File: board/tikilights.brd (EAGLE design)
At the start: 108.6 x 73 mm, 42 parts, among them IC1 AZ1117EH-3.3TRG1, SW1 ROTARTY_ENCODER, SW2 ROTARTY_ENCODER, SW3 ENCODER_SW1-PEC12, SW4 ENCODER_SW1-PEC12

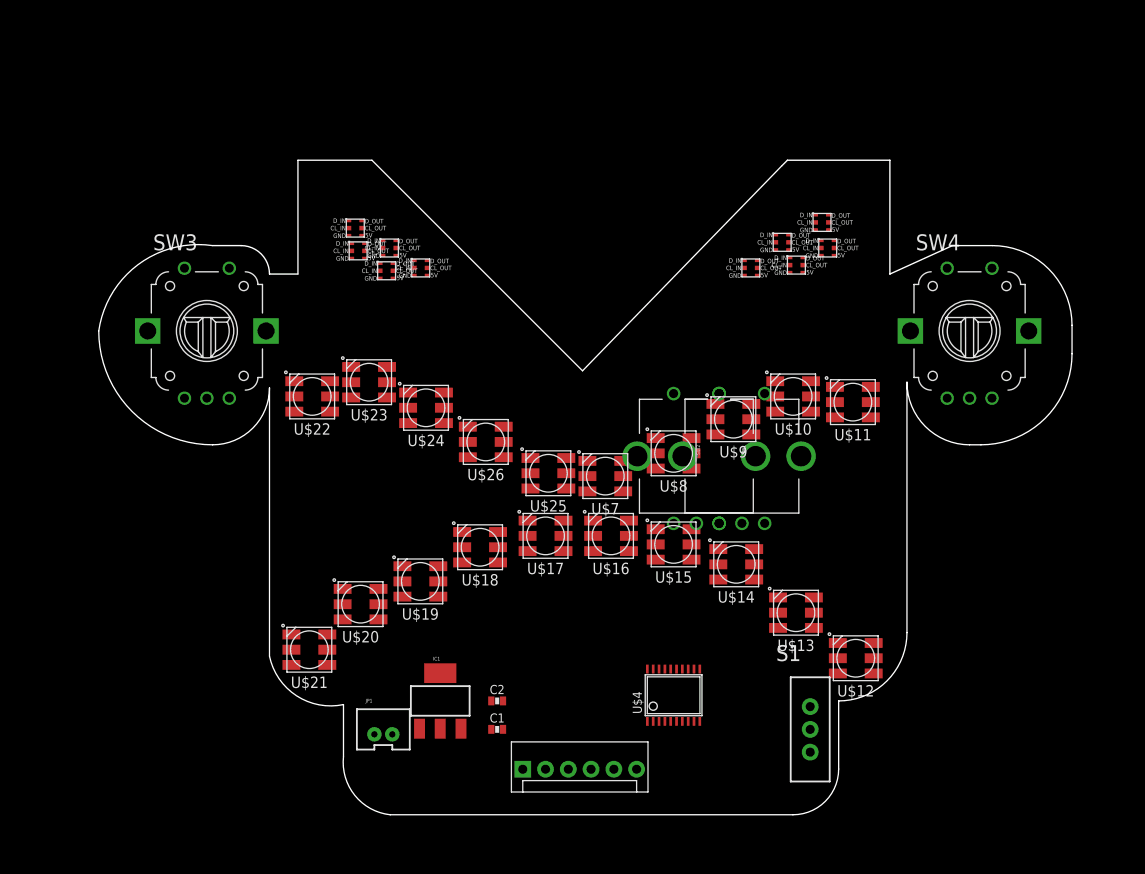
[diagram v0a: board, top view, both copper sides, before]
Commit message: Schematic is finished. Screw holes added. Need board layout and updated CAD model for dimensions.
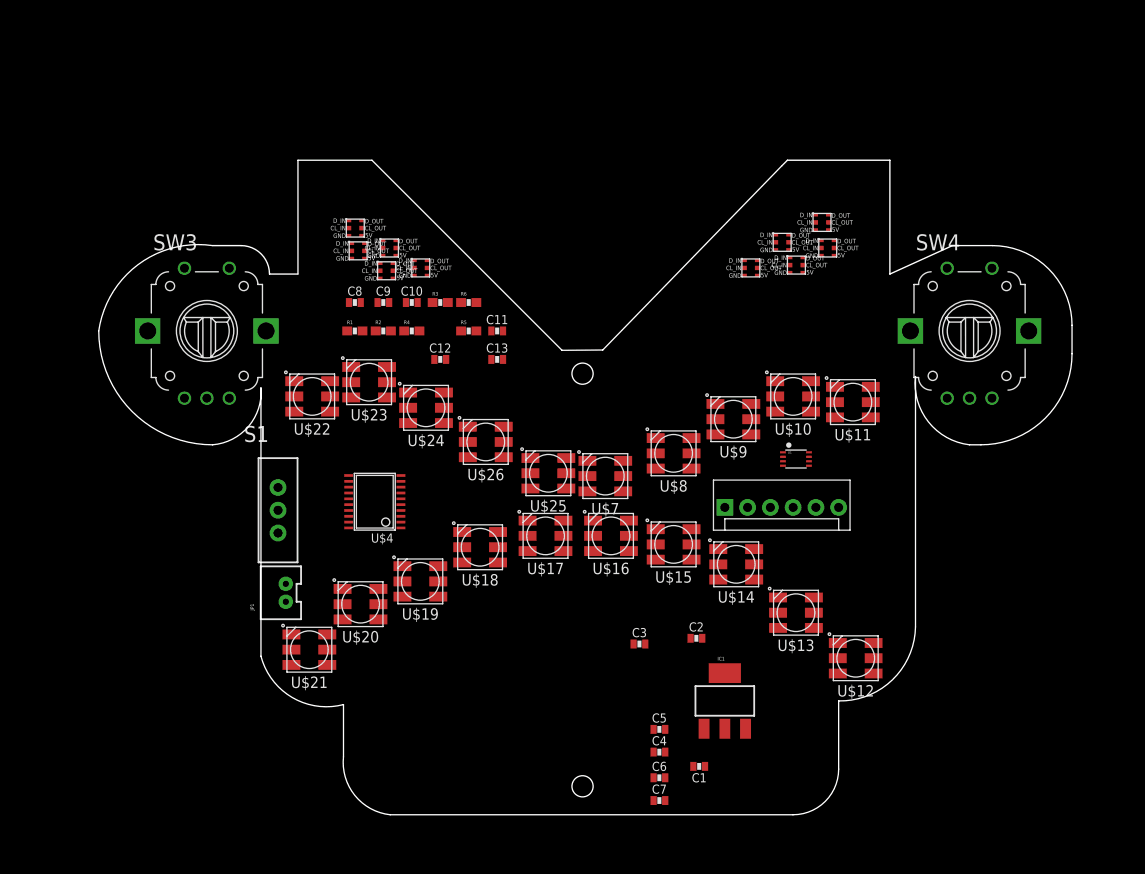
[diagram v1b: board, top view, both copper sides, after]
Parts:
- removed SW1, SW2: ROTARTY_ENCODER, SparkFun-Electromechanical:ROTARY_ENC_PLAIN
- added C10, C11, C12, C13, C8, C9: 0.1µF, passives:0603_CAP
- added C3, C4, C5, C6, C7: 1µF, passives:0603_CAP
- added R1, R2, R3, R4, R5, R6: (no value), SparkFun-Resistors:0603-RES
- added U1: (no value), adafruit:VFSOP-8
- moved S1 64.2 mm to (16.8, 34.0)
- moved U$4 39.7 mm to (27.6, 34.9), turned to 90 degrees
- moved JP3 36.9 mm to (66.7, 34.3)
- moved IC1 31.8 mm to (66.7, 12.7)
- moved C2 23.3 mm to (63.5, 19.7)
- moved C1 22.9 mm to (63.8, 5.40), turned to 180 degrees
- moved JP1 19.1 mm to (17.1, 24.8), turned to 90 degrees
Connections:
- new net BRIGHT_ROT_A: C8.1, R1.1, SW3.A, U$4.6
- new net BRIGHT_ROT_B: C10.1, R2.1, SW3.B, U$4.7
- new net BRIGHT_SWITCH: C9.1, R3.2, SW3.P1, U$4.8
- new net COLOR_ROT_A: C12.1, R5.1, SW4.A, U$4.10
- new net COLOR_ROT_B: C13.1, R4.1, SW4.B, U$4.9
- new net COLOR_SWITCH: C11.1, R6.2, SW4.P1, U$4.12
- new net LED_CLK: U$4.11, U1.P$4
- new net LED_CLK_5V: U$1.C_IN, U1.P$1
- new net LED_CLK_EYES: U$31.CL_OUT, U$7.5
- new net LED_CLK_MOUTH: U$16.2, U$17.5
- new net LED_DATA: U$4.13, U1.P$5
- new net LED_DATA_5V: U$1.D_IN, U1.P$8
- new net LED_DATA_EYES: U$31.D_OUT, U$7.4
- new net LED_DATA_MOUTH: U$16.3, U$17.4
- new net N$14: U$2.D_OUT, U$3.D_IN
- new net N$15: U$2.CL_OUT, U$3.C_IN
- new net N$16: U$3.D_OUT, U$5.D_IN
- new net N$17: U$3.CL_OUT, U$5.C_IN
- new net N$18: U$5.D_OUT, U$6.D_IN
- new net N$19: U$5.CL_OUT, U$6.C_IN
- new net N$20: U$27.D_IN, U$6.D_OUT
- new net N$21: U$27.C_IN, U$6.CL_OUT
- new net N$22: U$27.D_OUT, U$28.D_IN
- new net N$23: U$27.CL_OUT, U$28.C_IN
- new net N$24: U$28.D_OUT, U$29.D_IN
- new net N$25: U$28.CL_OUT, U$29.C_IN
- new net N$26: U$29.D_OUT, U$30.D_IN
- new net N$27: U$29.CL_OUT, U$30.C_IN
- new net N$28: U$30.D_OUT, U$31.D_IN
- new net N$29: U$30.CL_OUT, U$31.C_IN
- new net N$34: U$7.2, U$8.5
- new net N$35: U$7.3, U$8.4
- new net N$36: U$8.3, U$9.4
- new net N$37: U$8.2, U$9.5
- new net N$38: U$10.4, U$9.3
- new net N$39: U$10.5, U$9.2
- new net N$40: U$10.3, U$11.4
- new net N$41: U$10.2, U$11.5
- new net N$42: U$11.3, U$12.4
- new net N$43: U$11.2, U$12.5
- new net N$44: U$12.3, U$13.4
- new net N$45: U$12.2, U$13.5
- new net N$46: U$13.3, U$14.4
- new net N$47: U$13.2, U$14.5
- new net N$48: U$14.3, U$15.4
- new net N$49: U$14.2, U$15.5
- new net N$50: U$15.2, U$16.5
- new net N$51: U$15.3, U$16.4
- new net N$56: U$17.3, U$18.4
- new net N$57: U$17.2, U$18.5
- new net N$58: U$18.3, U$19.4
- new net N$59: U$18.2, U$19.5
- new net N$60: U$19.3, U$20.4
- new net N$61: U$19.2, U$20.5
- new net N$62: U$20.3, U$21.4
- new net N$63: U$20.2, U$21.5
- new net N$64: U$21.3, U$22.4
- new net N$65: U$21.2, U$22.5
- new net N$66: U$22.3, U$23.4
- new net N$67: U$22.2, U$23.5
- new net N$68: U$23.3, U$24.4
- new net N$69: U$23.2, U$24.5
- new net N$7: U$1.D_OUT, U$2.D_IN
- new net N$70: U$24.3, U$25.4
- new net N$71: U$24.2, U$25.5
- new net N$72: U$25.3, U$26.4
- new net N$73: U$25.2, U$26.5
- new net N$9: U$1.CL_OUT, U$2.C_IN
- new net NRST: JP3.2, U$4.4
- new net SWDCLK: JP3.5, U$4.20
- new net SWDIO: JP3.3, U$4.19
- net +5V: now also C7.1, U$1.V_CC, U$10.1, U$11.1, U$12.1, U$13.1, U$14.1, U$15.1, U$16.1, U$17.1, U$18.1, U$19.1, U$2.V_CC, U$20.1, U$21.1, U$22.1, U$23.1, U$24.1, U$25.1, U$26.1, U$27.V_CC, U$28.V_CC, U$29.V_CC, U$3.V_CC, U$30.V_CC, U$31.V_CC, U$5.V_CC, U$6.V_CC, U$7.1, U$8.1, U$9.1, U1.P$7
- net 3.3V: now also C3.1, C4.1, C5.1, C6.1, JP3.6, R1.2, R2.2, R4.2, R5.2, SW3.P2, SW4.P2, U$4.16, U$4.5, U1.P$3
- net GND: now also C10.2, C11.2, C12.2, C13.2, C3.2, C4.2, C5.2, C6.2, C7.2, C8.2, C9.2, JP3.4, R3.1, R6.1, SW3.C, SW4.C, U$1.GND, U$10.6, U$11.6, U$12.6, U$13.6, U$14.6, U$15.6, U$16.6, U$17.6, U$18.6, U$19.6, U$2.GND, U$20.6, U$21.6, U$22.6, U$23.6, U$24.6, U$25.6, U$26.6, U$27.GND, U$28.GND, U$29.GND, U$3.GND, U$30.GND, U$31.GND, U$4.15, U$5.GND, U$6.GND, U$7.6, U$8.6, U$9.6, U1.P$2, U1.P$6
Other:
- outline, holes or cut-outs redrawn

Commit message: Updating board to fit resized mask. Battery pack now fits and everything is in place for routing. Mask still needs a hook, and board needs a message.
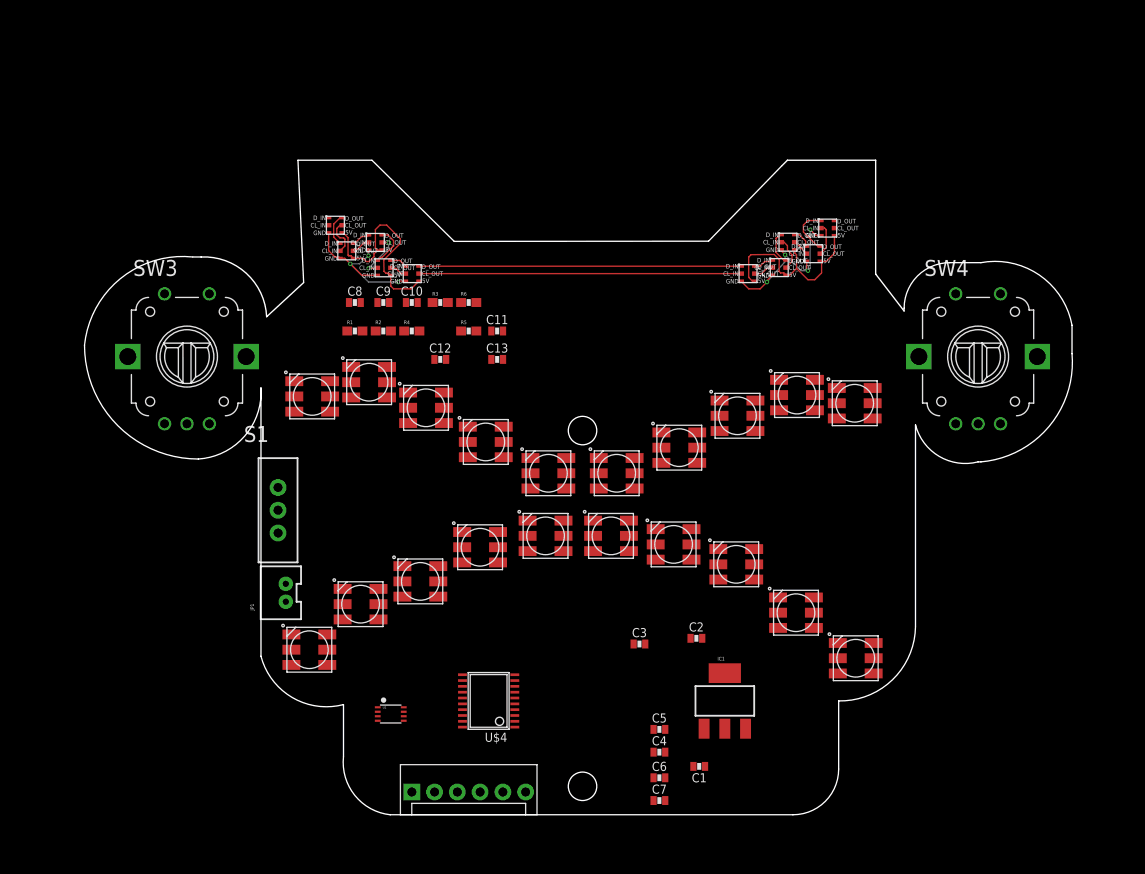
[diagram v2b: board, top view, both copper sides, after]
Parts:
- moved U1 53.4 mm to (29.4, 11.2)
- moved JP3 47.2 mm to (31.8, 2.54)
- moved U$34 46.5 mm to (-3.49, -7.94)
- moved U$4 25.6 mm to (40.3, 12.7)
- moved U$30 3.62 mm to (75.6, 61.6)
- moved SW3 3.62 mm to (6.67, 51.1)
- moved U$3 3.40 mm to (26.7, 62.9)
- moved SW4 3.01 mm to (94.9, 51.1)
- moved U$28 2.84 mm to (71.7, 60.0)
- moved U$29 2.72 mm to (72.7, 62.9)
- moved U$5 2.29 mm to (27.7, 60.0)
- moved U$1 2.25 mm to (22.2, 64.8)
- moved U$31 2.22 mm to (77.2, 64.5)
- moved U$7 1.31 mm to (54.6, 38.1)
- moved U$2 1.27 mm to (23.5, 61.9)
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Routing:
- net +5V: track 0.00 -> 45.6 mm
- net GND: track 0.00 -> 38.4 mm, vias 0 -> 7
- net N$21: track 0.00 -> 36.0 mm
- net N$20: track 0.00 -> 36.0 mm
- net N$17: track 0.00 -> 5.55 mm, vias 0 -> 2
- net N$28: track 0.00 -> 5.49 mm
- net N$16: track 0.00 -> 4.58 mm
- net N$9: track 0.00 -> 4.09 mm
- net N$25: track 0.00 -> 3.79 mm
- net N$24: track 0.00 -> 3.74 mm
- net N$7: track 0.00 -> 3.68 mm
- net N$29: track 0.00 -> 3.61 mm
- net N$22: track 0.00 -> 2.26 mm
- net N$23: track 0.00 -> 2.26 mm
- net N$26: track 0.00 -> 2.15 mm
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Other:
- board size 108.6 x 73 mm -> 110.2 x 73 mm

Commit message: Adjusting lights positioning.
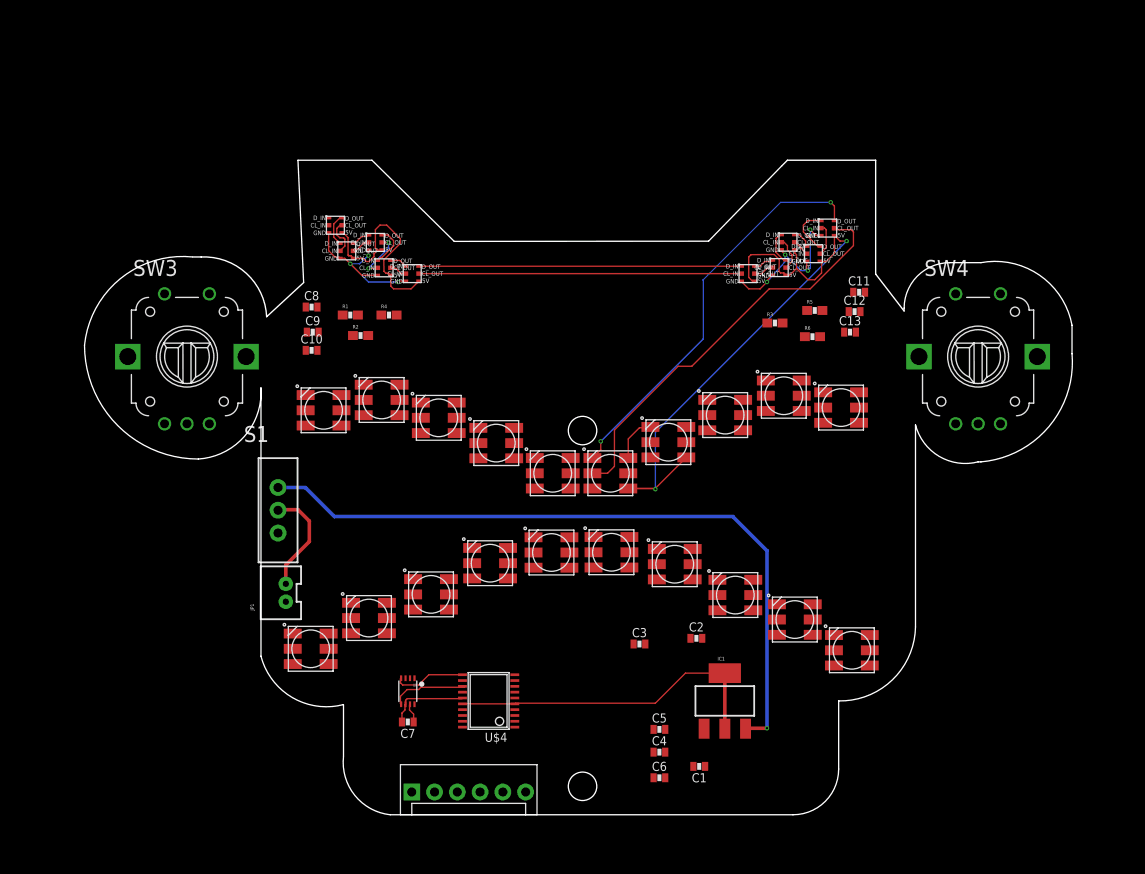
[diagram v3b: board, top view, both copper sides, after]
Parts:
- moved C12 46.5 mm to (81.2, 56.1)
- moved C11 40.6 mm to (81.7, 58.3)
- moved C13 39.5 mm to (80.6, 53.8)
- moved R5 38.7 mm to (76.7, 56.3)
- moved R6 38.5 mm to (76.5, 53.3)
- moved R3 37.4 mm to (72.3, 54.9)
- moved C7 29.4 mm to (31.3, 10.4), turned to 180 degrees
- moved C10 12.4 mm to (20.6, 51.8)
- moved C9 8.54 mm to (20.7, 53.8)
- moved C8 4.85 mm to (20.6, 56.6)
- moved U$14 3.43 mm to (67.8, 24.5)
- moved U1 3.17 mm to (31.3, 13.8), turned to 180 degrees
- moved R4 3.10 mm to (29.2, 55.8)
- moved R2 2.59 mm to (26.0, 53.5)
- moved U$23 2.42 mm to (28.4, 46.3)
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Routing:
- net +5V: track 45.6 -> 176.6 mm, vias 0 -> 3
- net LED_CLK_EYES: track 0.24 -> 46.2 mm
- net LED_DATA_EYES: track 0.00 -> 45.0 mm, vias 0 -> 2
- net 3.3V: track 0.00 -> 36.9 mm
- net VCC: track 0.00 -> 12.1 mm
- net GND: track 38.4 -> 47.4 mm
- net LED_DATA: track 0.00 -> 8.67 mm
- net LED_CLK: track 0.00 -> 8.03 mm
- net N$35: track 0.00 -> 5.16 mm

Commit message: Submitting tikilights v1. Both board and cad. Hope I didn't forget anything!
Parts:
- added U$32: (no value), tikilights:KOALA
- R1, R2, R3, R4, R5, R6: value (none) -> 10k
- S1: value (none) -> SPDT
- U1: value (none) -> AZ1117E
- moved R3 37.1 mm to (35.4, 50.3), turned to 180 degrees
- moved R4 35.4 mm to (64.3, 50.7), turned to 180 degrees
- moved R5 12.5 mm to (64.3, 55.5), turned to 180 degrees
- moved C12 12.2 mm to (69.7, 51.8), turned to 180 degrees
- moved C11 12.2 mm to (69.7, 55.8), turned to 180 degrees
- moved R6 12.2 mm to (64.3, 53.1)
- moved C13 10.9 mm to (69.7, 53.8), turned to 180 degrees
- moved C10 10.7 mm to (31.2, 50.5)
- moved C8 10.7 mm to (31.2, 55.6)
- moved C9 10.7 mm to (31.4, 53.1)
- moved R1 10.4 mm to (35.3, 55.5)
- moved R2 9.43 mm to (35.4, 52.7)
- moved C3 7.71 mm to (59.4, 11.7)
- moved U$26 7.15 mm to (47.5, 38.1)
- moved C2 7.12 mm to (59.4, 13.8)
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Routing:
- net GND: track 47.4 -> 431.4 mm, vias 7 -> 29
- net +5V: track 176.6 -> 477.6 mm, vias 3 -> 18
- net 3.3V: track 36.9 -> 277.1 mm, vias 0 -> 3
- net COLOR_ROT_B: track 0.00 -> 150.6 mm, vias 0 -> 5
- net BRIGHT_ROT_A: track 0.00 -> 124.8 mm, vias 0 -> 2
- net COLOR_ROT_A: track 0.00 -> 92.7 mm, vias 0 -> 4
- net BRIGHT_SWITCH: track 0.00 -> 92.0 mm, vias 0 -> 3
- net COLOR_SWITCH: track 0.00 -> 88.7 mm, vias 0 -> 6
- net BRIGHT_ROT_B: track 0.00 -> 85.0 mm, vias 0 -> 2
- net LED_DATA_5V: track 0.00 -> 77.2 mm, vias 0 -> 2
- net LED_CLK_5V: track 0.00 -> 69.1 mm, vias 0 -> 2
- net N$64: track 0.00 -> 38.7 mm
- net N$42: track 0.00 -> 34.7 mm
- net N$65: track 0.00 -> 34.6 mm
- net N$43: track 0.00 -> 30.2 mm
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- added copper zone on layer 1, net GND
- added copper zone on layer 16, net GND
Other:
- board size 110.2 x 73 mm -> 106.4 x 72.5 mm
- board text added: "Happy 33rd Birthday Brittany!"
- board text added: "Let's take a moment, look around, and recognize how wonderful it is that we found each other and have made a life together. Yours forever, Sammy"

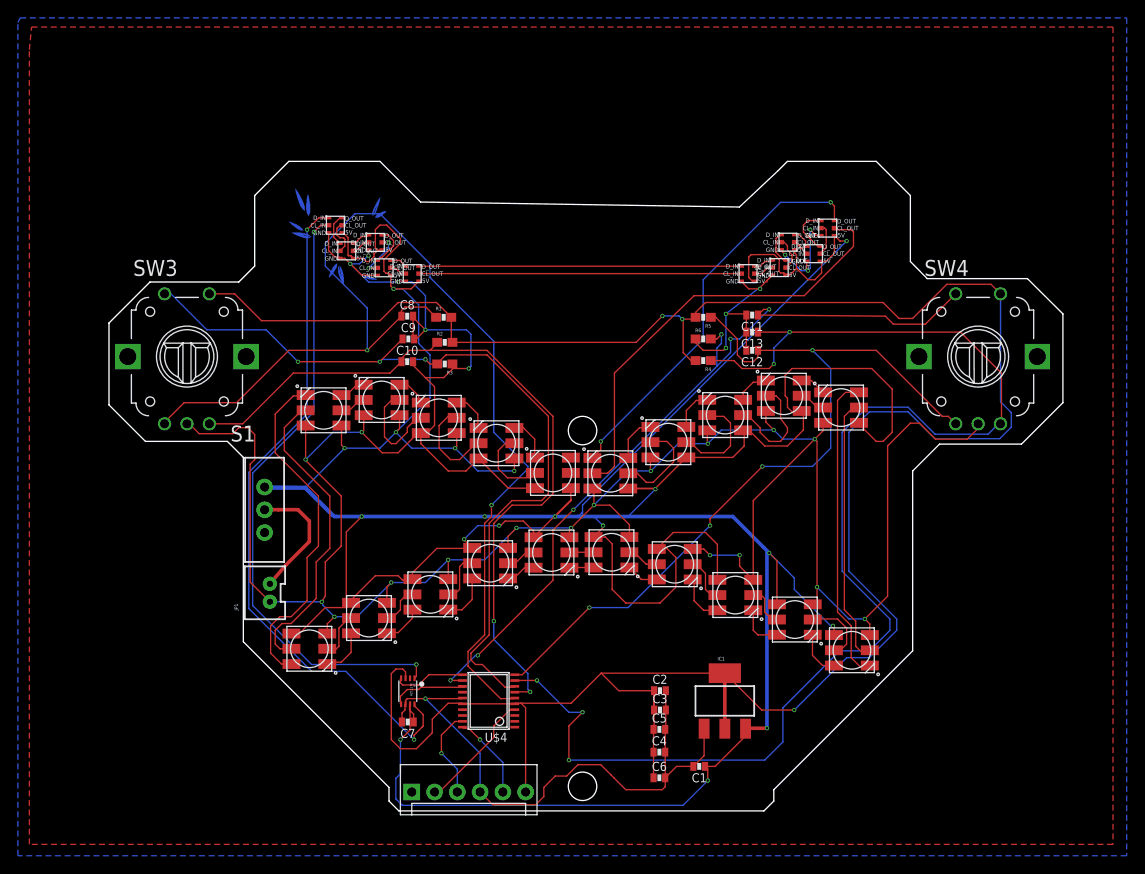
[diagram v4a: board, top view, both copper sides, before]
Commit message: Revision 2. Fixing TXB0102 board. Widening encoder side drill holes.
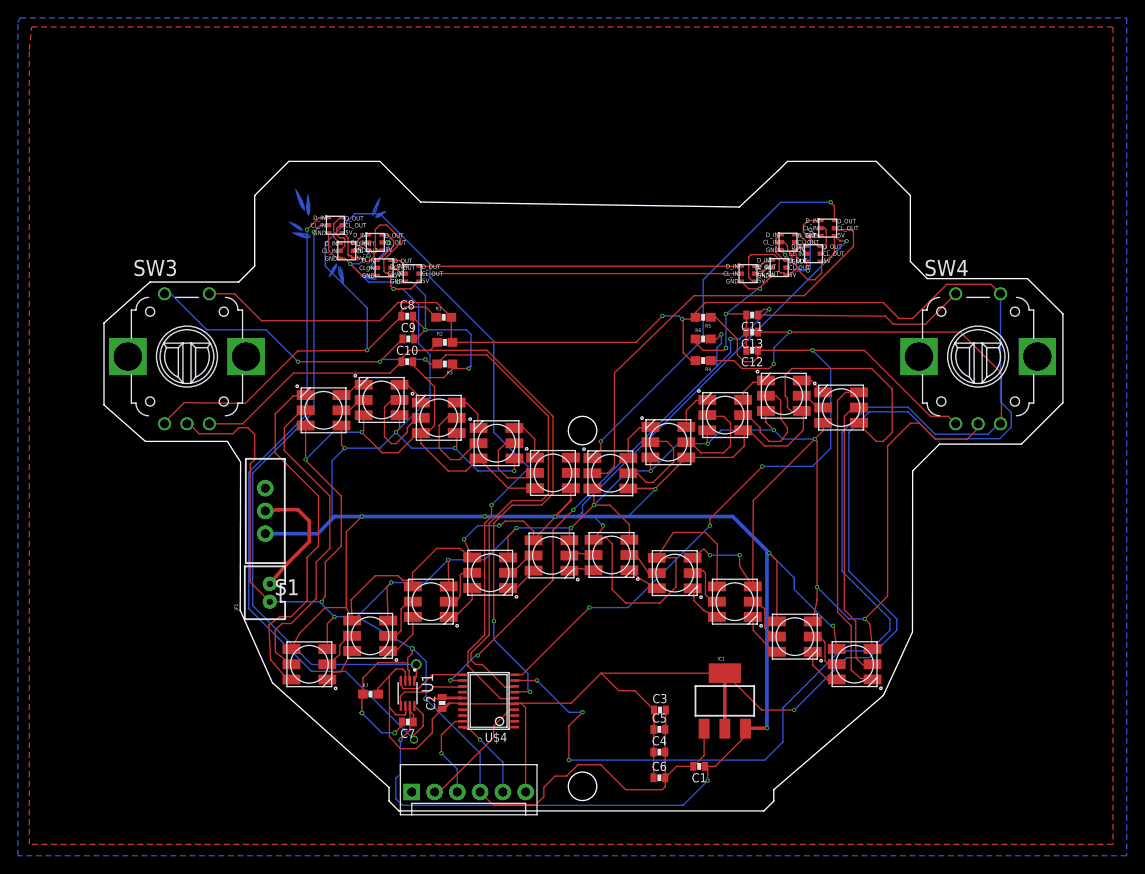
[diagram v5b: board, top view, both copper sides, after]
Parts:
- added R7: 10k, SparkFun-Resistors:0603-RES
- U1: value AZ1117E -> TXB0102; device adafruit:VFSOP-8 -> TXB0102:SOP50P310X90-8N
- moved C2 24.3 mm to (35.1, 12.5), turned to 90 degrees
- moved U$20 1.99 mm to (27.1, 20.0)
- moved U$13 1.91 mm to (74.5, 19.9)
- moved U$21 1.73 mm to (20.3, 16.8)
- moved U$12 1.58 mm to (81.2, 16.8)
- moved U$18 1.07 mm to (40.5, 27.0)
- moved U$15 0.99 mm to (61.1, 27.0)
- moved U$19 0.81 mm to (33.9, 23.8)
- moved U$14 0.74 mm to (67.8, 23.8)
- moved U$17 0.33 mm to (47.3, 28.9)
- moved U$16 0.30 mm to (54.0, 29.0)
- moved U1 0.23 mm to (31.3, 13.6), turned to 270 degrees
- moved S1 0.15 mm to (15.4, 33.9), turned to 180 degrees
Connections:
- net +5V: now also U1.7; no longer U1.P$7
- net 3.3V: now also R7.2, U1.3, U1.6; no longer U1.P$3
- net GND: now also R7.1, U1.2; no longer U1.P$2, U1.P$6
- net LED_CLK: now also U1.4; no longer U1.P$4
- net LED_CLK_5V: now also U1.1; no longer U1.P$1
- net LED_DATA: now also U1.5; no longer U1.P$5
- net LED_DATA_5V: now also U1.8; no longer U1.P$8
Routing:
- net GND: track 431.4 -> 470.9 mm, vias 29 -> 32
- net +5V: track 477.6 -> 481.5 mm
- net 3.3V: track 277.1 -> 281.0 mm
- net N$45: track 7.71 -> 5.17 mm
- net N$42: track 34.7 -> 36.2 mm
- net N$43: track 30.2 -> 31.7 mm
- net N$64: track 38.7 -> 40.1 mm
- net N$61: track 4.62 -> 5.76 mm
- net N$65: track 34.6 -> 35.7 mm
- net N$60: track 4.51 -> 5.47 mm
- net N$48: track 5.48 -> 4.57 mm
- net N$63: track 5.44 -> 4.62 mm
- net N$50: track 3.61 -> 4.41 mm
- net N$47: track 4.67 -> 5.43 mm
- net N$62: track 5.29 -> 4.53 mm
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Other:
- board size 106.4 x 72.5 mm -> 107 x 72.5 mm
- board text added: "Let this tiki god bathe you with light. I hope we have many adventures lit by his fearsome mouth. Yours forever, Sammy April 18th, 2018"
- board text removed: "Let's take a moment, look around, and recognize how wonderful it is that we found each other and have made a life together. Yours forever, Sammy"
